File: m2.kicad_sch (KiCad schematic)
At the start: 61 parts, among them J13 Bus_M.2_1-2199230-6, J14 Bus_M.2_2199230-2, Y3 Oscillator_32.768kHz_ECS_2520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

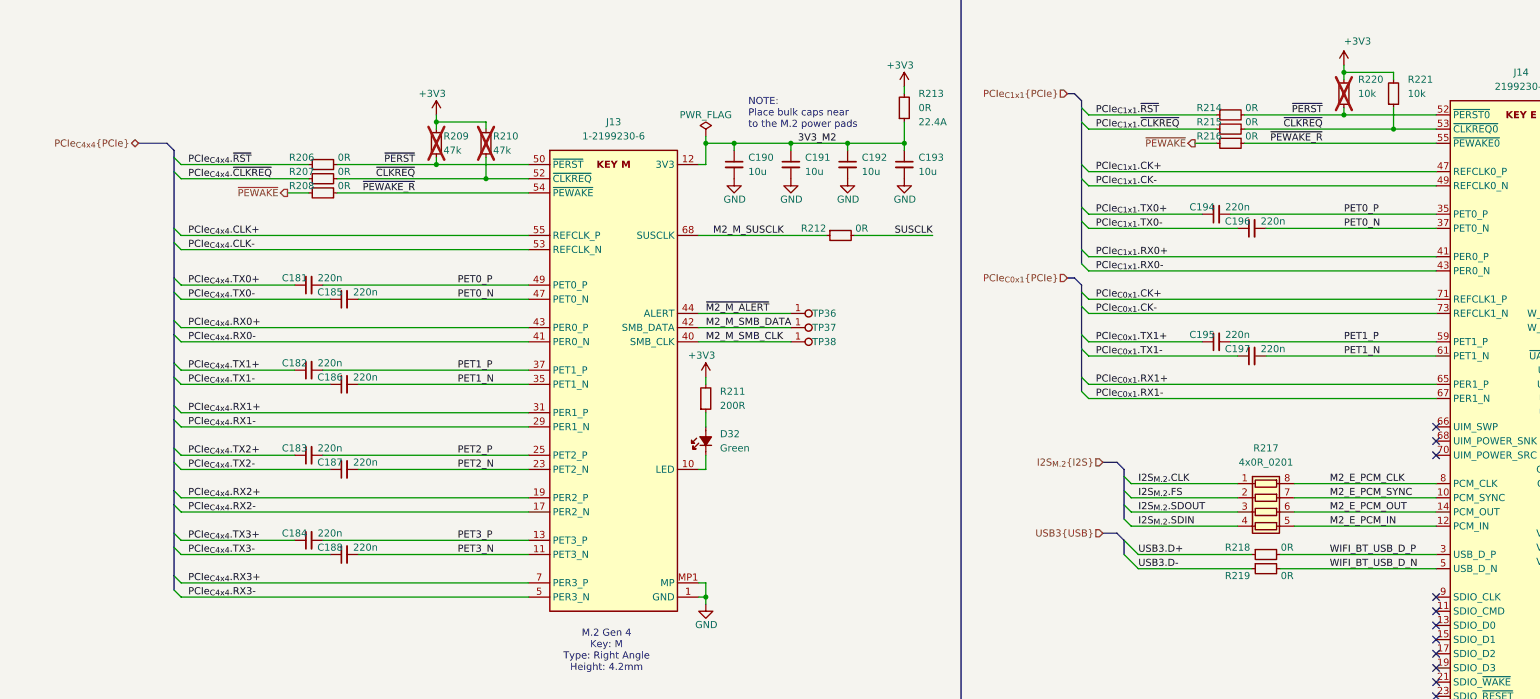
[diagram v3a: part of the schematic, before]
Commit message: [#82837] Finish mapping interfaces, waiting for new SoM symbol
[#82837] Add GPIO level shifter and route USB related GPIO on root
schematic

[#82837] WIP: Modify Power-up and reset section
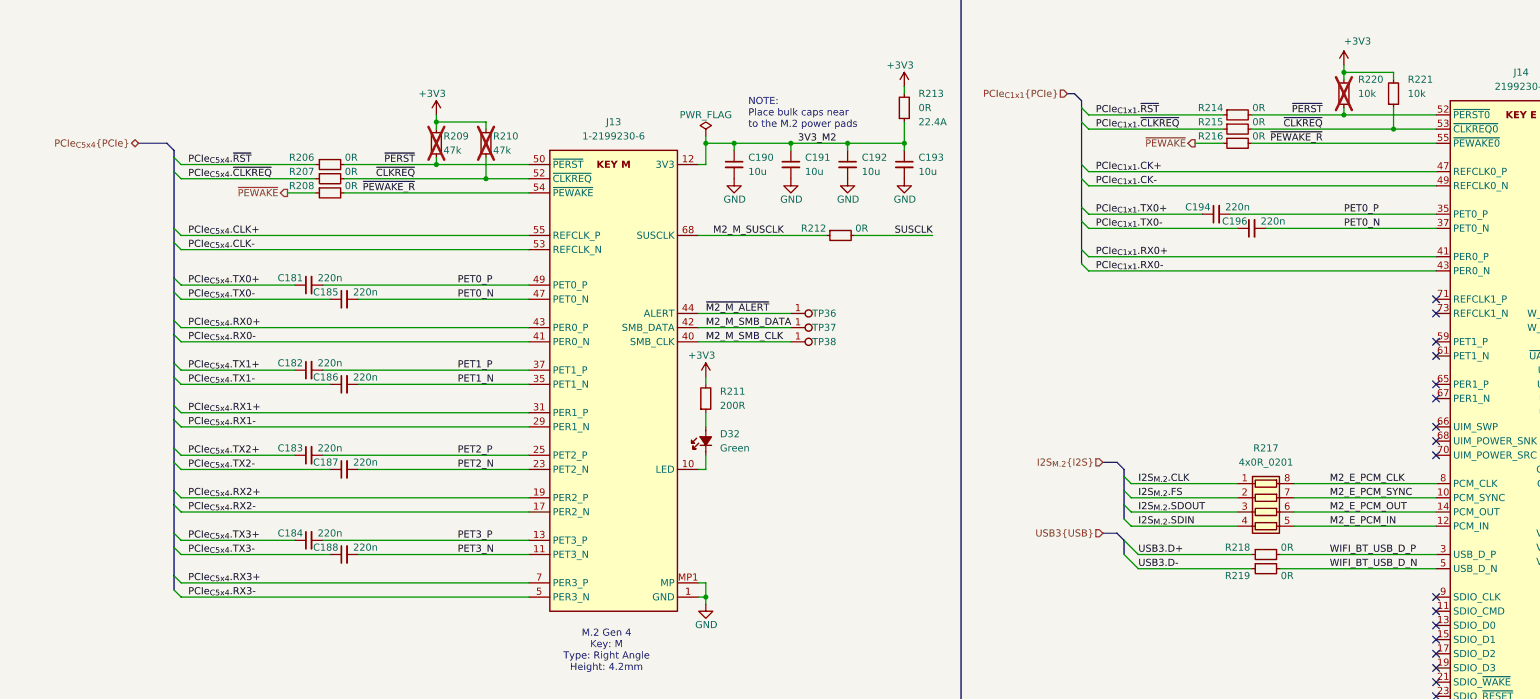
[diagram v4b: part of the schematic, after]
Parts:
- removed C195, C197: C_220n_6V3_X7R_0402, antmicro-footprints:C_0402_1005Metric, symbol antmicroCapacitors0402:C_220n_6V3_X7R_0402
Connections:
- net PET1_N: no longer J14.61 (PET1_N)
- net PET1_P: no longer J14.59 (PET1_P)
- net PCIe_{C0x1}.CK+: no longer names the net of J14.71 (REFCLK1_P)
- net PCIe_{C0x1}.CK-: no longer names the net of J14.73 (REFCLK1_N)
- net PCIe_{C0x1}.RX1+: no longer names the net of J14.65 (PER1_P)
- net PCIe_{C0x1}.RX1-: no longer names the net of J14.67 (PER1_N)
- net PCIe_{C4x4}.CLK+ renamed PCIe_{C5x4}.CLK+
- net PCIe_{C4x4}.CLK- renamed PCIe_{C5x4}.CLK-
- net PCIe_{C4x4}.RX0+ renamed PCIe_{C5x4}.RX0+
- net PCIe_{C4x4}.RX0- renamed PCIe_{C5x4}.RX0-
- net PCIe_{C4x4}.RX1+ renamed PCIe_{C5x4}.RX1+
- net PCIe_{C4x4}.RX1- renamed PCIe_{C5x4}.RX1-
- net PCIe_{C4x4}.RX2+ renamed PCIe_{C5x4}.RX2+
- net PCIe_{C4x4}.RX2- renamed PCIe_{C5x4}.RX2-
- net PCIe_{C4x4}.RX3+ renamed PCIe_{C5x4}.RX3+
- net PCIe_{C4x4}.RX3- renamed PCIe_{C5x4}.RX3-
- net PCIe_{C4x4}.TX0+ renamed PCIe_{C5x4}.TX0+
- net PCIe_{C4x4}.TX0- renamed PCIe_{C5x4}.TX0-
- net PCIe_{C4x4}.TX1+ renamed PCIe_{C5x4}.TX1+
- net PCIe_{C4x4}.TX1- renamed PCIe_{C5x4}.TX1-
- net PCIe_{C4x4}.TX2+ renamed PCIe_{C5x4}.TX2+
- net PCIe_{C4x4}.TX2- renamed PCIe_{C5x4}.TX2-
- net PCIe_{C4x4}.TX3+ renamed PCIe_{C5x4}.TX3+
- net PCIe_{C4x4}.TX3- renamed PCIe_{C5x4}.TX3-
- net PCIe_{C4x4}.~{CLKREQ} renamed PCIe_{C5x4}.~{CLKREQ}
- net PCIe_{C4x4}.~{RST} renamed PCIe_{C5x4}.~{RST}
- no-connect marks 17 -> 23
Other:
- moved on the sheet: R206, R207, R208, R214, R215, R216

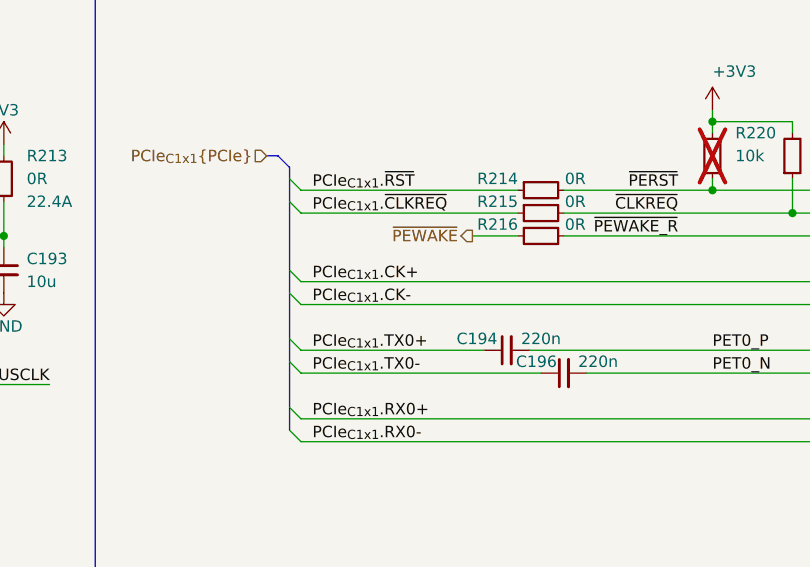
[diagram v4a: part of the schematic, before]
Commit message: [#82837] Swap SoM form AGX Orin to Thor with all of its connections
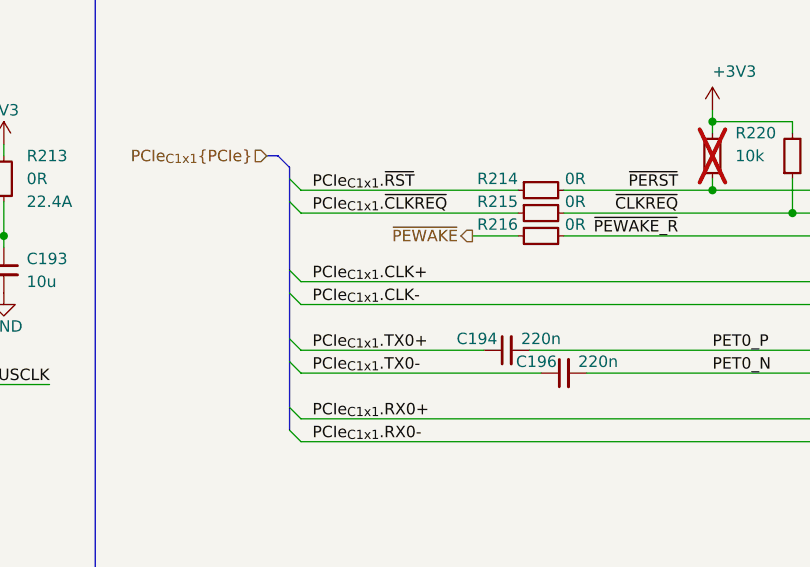
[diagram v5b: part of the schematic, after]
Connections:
- net PCIe_{C1x1}.CK+ renamed PCIe_{C1x1}.CLK+
- net PCIe_{C1x1}.CK- renamed PCIe_{C1x1}.CLK-
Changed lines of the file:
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@@
 		)
 	)
-	(label "PCIe_{C1x1}.CK-"
+	(label "PCIe_{C1x1}.CLK-"
 		(at 201.93 106.68 0)
 		(effects
@@
 		)
 	)
-	(label "PCIe_{C1x1}.CK+"
+	(label "PCIe_{C1x1}.CLK+"
 		(at 201.93 104.14 0)
 		(effects

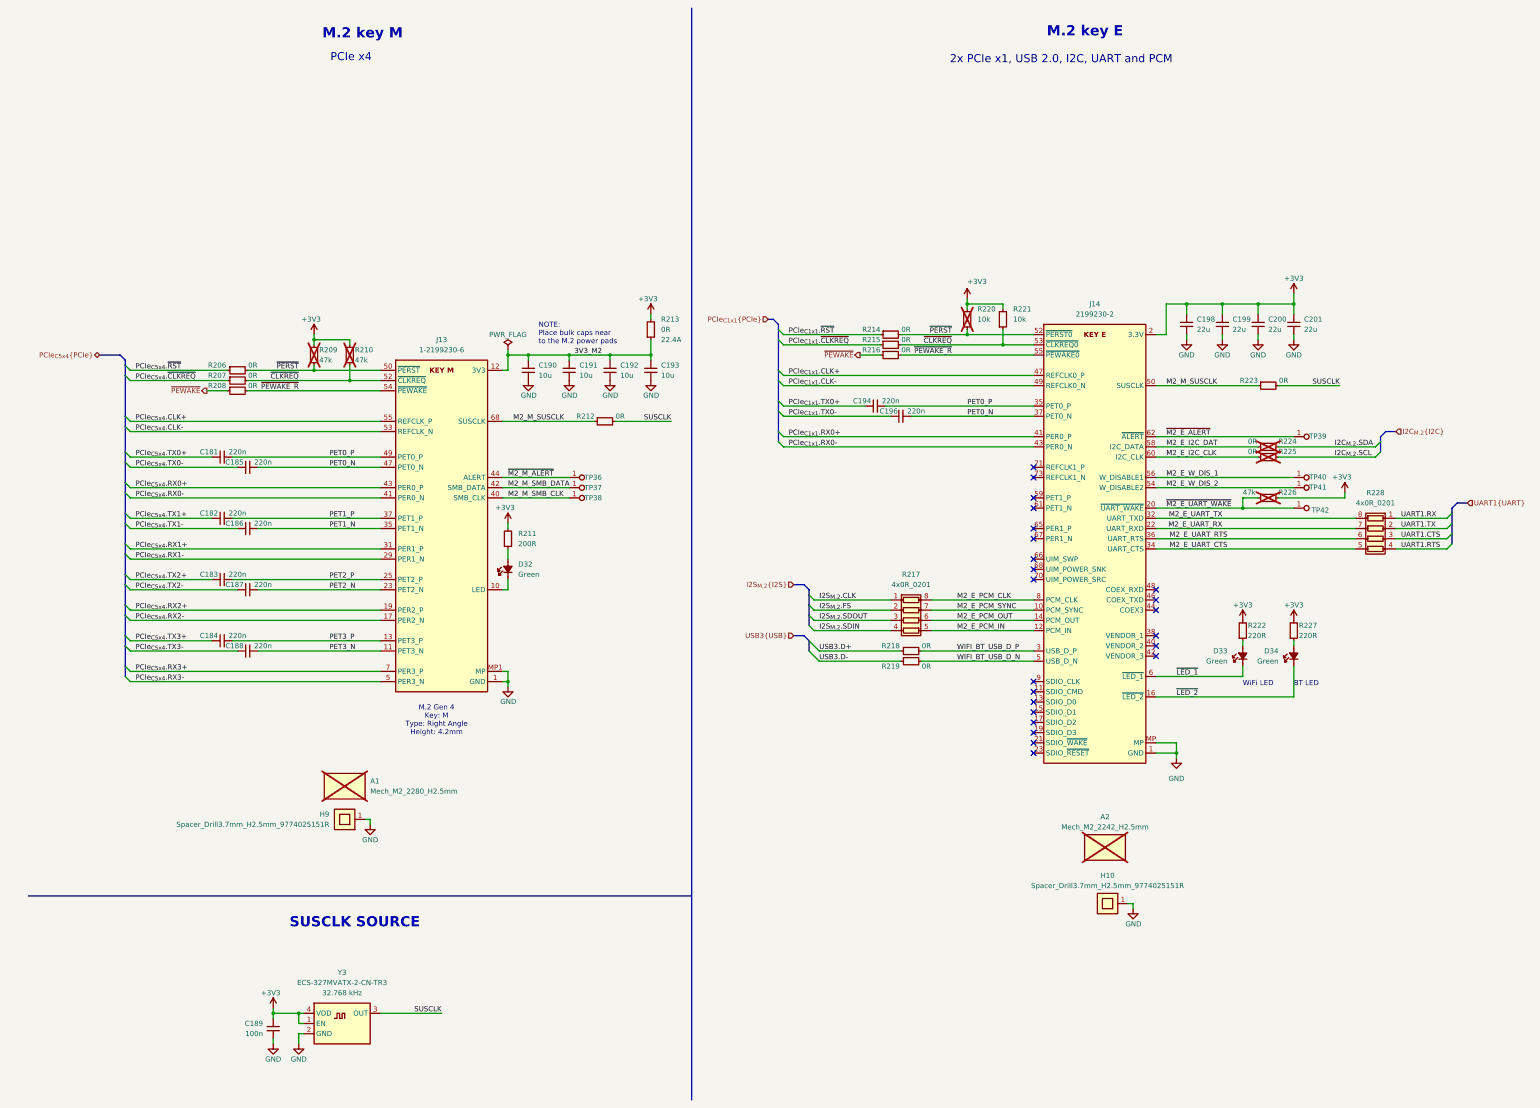
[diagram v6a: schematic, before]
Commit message: [#82837] Finish mapping PCIe and SFP+ connections on SoM
[#82837] WIP: correct ERC errors

[#82837] WIP: correct ERC errors, fix signal direction of most buses

[#82837] Fix all ERC errors
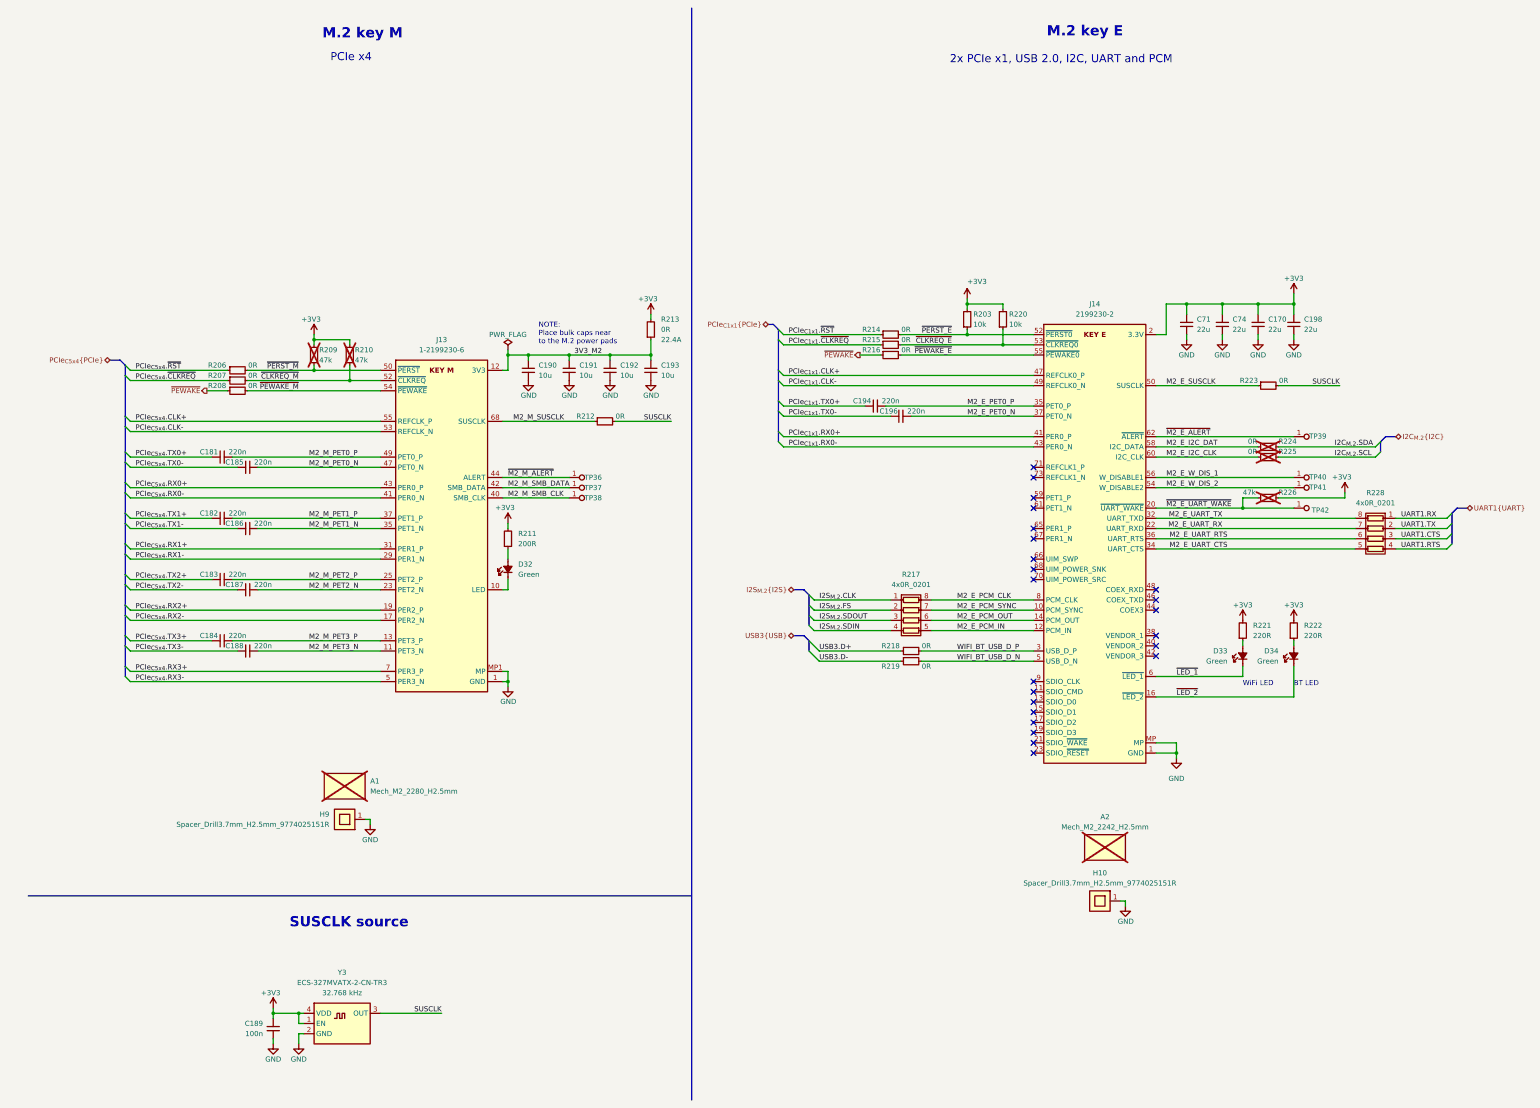
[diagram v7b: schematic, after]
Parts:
- removed C198, C199, C200, C201: C_22u_16V_0603, antmicro-footprints:C_0603_1608Metric, symbol antmicroCapacitors0603:C_22u_16V_0603
- removed R221: R_10k_0402, antmicro-footprints:R_0402_1005Metric, symbol antmicroResistors0402:R_10k_0402
- removed R227: R_220R_0402, antmicro-footprints:R_0402_1005Metric, symbol antmicroResistors0402:R_220R_0402
- added C170, C198, C71, C74: C_22u_10V_0603, antmicro-footprints:C_0603_1608Metric, symbol antmicroCapacitors0603:C_22u_10V_0603
- added R203: R_10k_0402, antmicro-footprints:R_0402_1005Metric, symbol antmicroResistors0402:R_10k_0402
- added R221: R_220R_0402, antmicro-footprints:R_0402_1005Metric, symbol antmicroResistors0402:R_220R_0402
- R220: Public False -> (none); now fitted
- R222: Public False -> (none)
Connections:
- net +3V3: now also C170.2, C198.2, C71.2, C74.2, R203.2, R221.2
- net GND: now also C170.1, C198.1, C71.1, C74.1
- net M2_M_SUSCLK: no longer J14.50 (SUSCLK), R223.1
- net at R222.1: now also D34.2 (A); no longer D33.2 (A)
- net PET0_N renamed M2_E_PET0_N
- net M2_E_PET0_N: no longer C185.2, J13.47 (PET0_N)
- net PET0_P renamed M2_E_PET0_P
- net M2_E_PET0_P: no longer C181.2, J13.49 (PET0_P)
- net PET1_N renamed M2_M_PET1_N
- net PET1_P renamed M2_M_PET1_P
- net PET2_N renamed M2_M_PET2_N
- net PET2_P renamed M2_M_PET2_P
- net PET3_N renamed M2_M_PET3_N
- net PET3_P renamed M2_M_PET3_P
- net ~{CLKREQ} renamed ~{CLKREQ_M}
- net ~{CLKREQ_M}: no longer J14.53 (~{CLKREQ0}), R215.2
- net ~{PERST} renamed ~{PERST_M}
- net ~{PERST_M}: no longer J14.52 (~{PERST0}), R214.2, R220.1
- net ~{PEWAKE_R} renamed ~{PEWAKE_E}
- net ~{PEWAKE_E}: no longer J13.54 (~{PEWAKE}), R208.2
- new net: D33.2 (A), R221.1
- new net M2_E_SUSCLK: J14.50 (SUSCLK), R223.1
- new net M2_M_PET0_N: C185.2, J13.47 (PET0_N)
- new net M2_M_PET0_P: C181.2, J13.49 (PET0_P)
- new net ~{CLKREQ_E}: J14.53 (~{CLKREQ0}), R215.2, R220.1
- new net ~{PERST_E}: J14.52 (~{PERST0}), R203.1, R214.2
- new net ~{PEWAKE_M}: J13.54 (~{PEWAKE}), R208.2
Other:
- note added: "SUSCLK source"
- note removed: "M.2 Gen 4 Key: M Type: Right Angle Height: 4.2mm"
- note removed: "SUSCLK SOURCE"
- moved on the sheet: H10

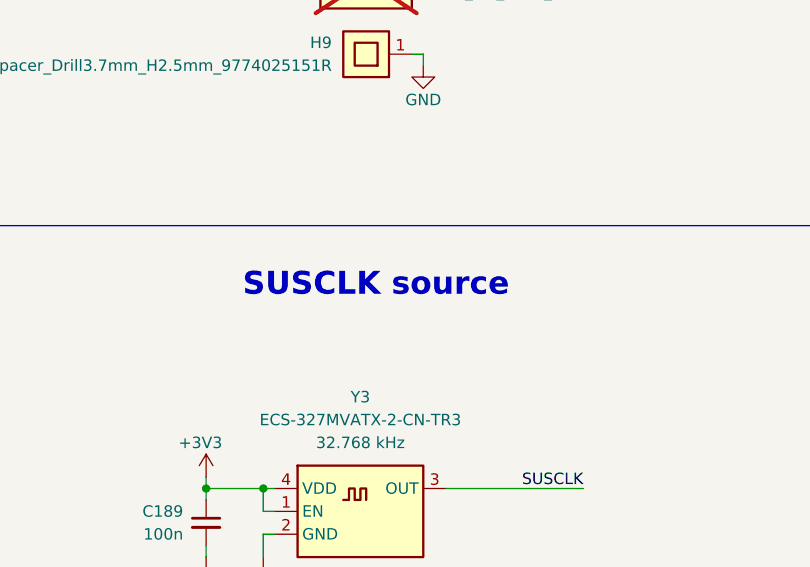
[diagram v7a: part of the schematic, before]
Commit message: [#83224] Import all of the components to PCB and divide them into functional groups
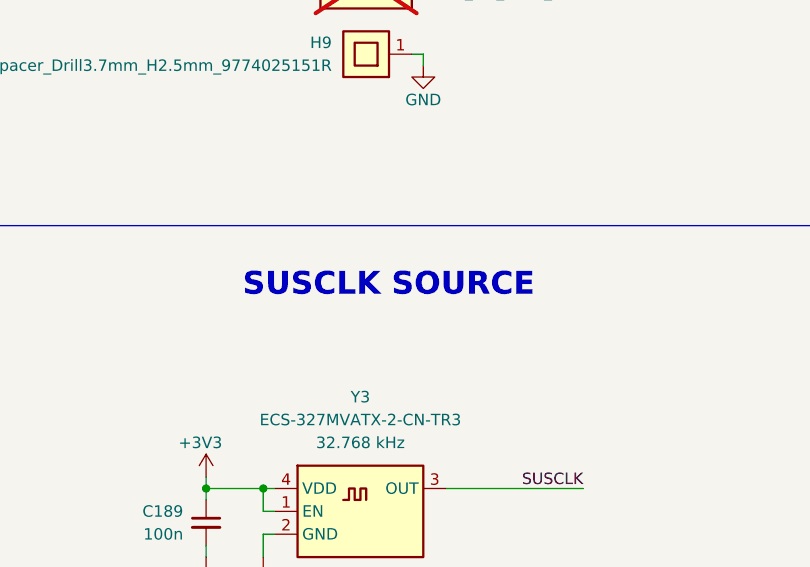
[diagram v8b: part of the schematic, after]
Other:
- note added: "SUSCLK SOURCE"
- note removed: "SUSCLK source"
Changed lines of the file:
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@@
 		)
 	)
-	(text "SUSCLK source"
+	(text "SUSCLK SOURCE"
 		(exclude_from_sim no)
 		(at 77.724 241.808 0)
